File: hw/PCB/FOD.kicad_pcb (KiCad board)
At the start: 2 copper layers, 82.5 x 29 mm, 44 parts, among them J1 USB_B_Micro, J2 I2C, J3 I2C, J4 Programmer, J5 Micro_SD_Card_Det, J6 U.FL, Q1 PMV16XNR, Q2 PMV16XNR, SW1 Reset_push, U1 SAMD21G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

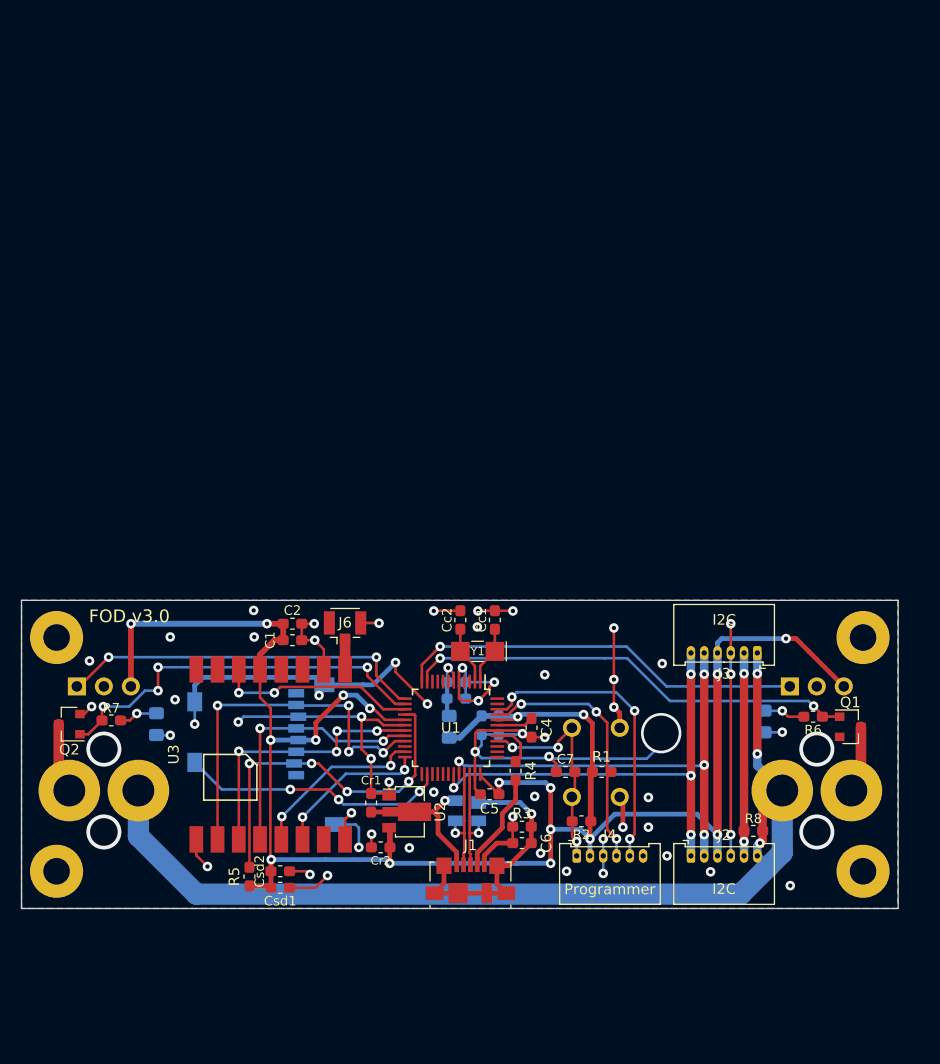
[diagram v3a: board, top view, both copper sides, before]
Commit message: FOD's new PCB version.
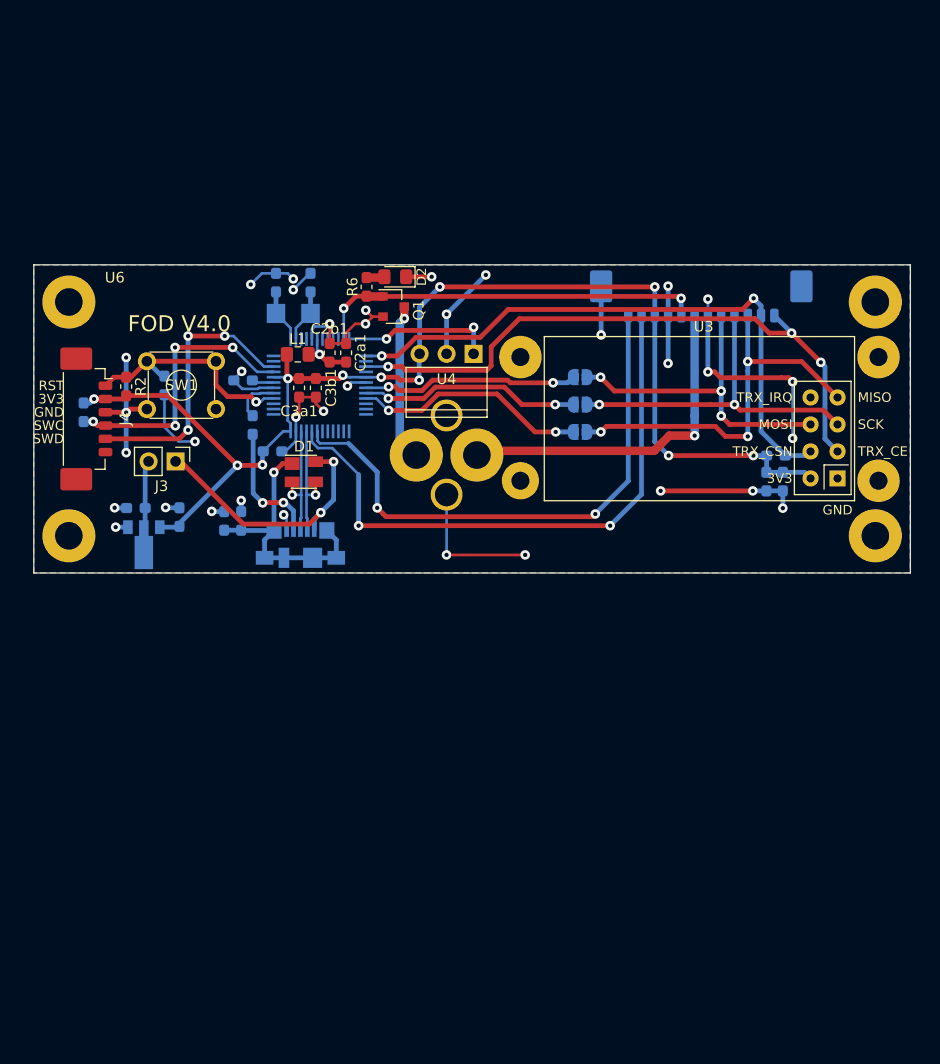
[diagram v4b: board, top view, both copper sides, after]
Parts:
- removed C1, Csd1: 10uF, Capacitor_SMD:C_0603_1608Metric_Pad1.05x0.95mm_HandSolder
- removed C2: 0.1uF, Capacitor_SMD:C_0603_1608Metric_Pad1.05x0.95mm_HandSolder
- removed Csd2: 100nF, Capacitor_SMD:C_0603_1608Metric_Pad1.05x0.95mm_HandSolder
- removed D3: LED, Diode_SMD:D_0805_2012Metric_Pad1.15x1.40mm_HandSolder
- removed J5: Micro_SD_Card_Det, SD:microSD_socket
- removed J6: U.FL, Connector_Coaxial:U.FL_Hirose_U.FL-R-SMT-1_Vertical
- removed Q2: PMV16XNR, Package_TO_SOT_SMD:SOT-23
- removed R5: 100k, Resistor_SMD:R_0603_1608Metric_Pad1.05x0.95mm_HandSolder
- removed R8: 0, Resistor_SMD:R_0603_1608Metric_Pad1.05x0.95mm_HandSolder
- removed U5: AV4524, Interrupt:AV4524
- added Ct1: 0.1uF, Capacitor_SMD:C_0603_1608Metric_Pad1.05x0.95mm_HandSolder, B.Cu at (170.1, 68.8)
- added Ct2: 10uF, Capacitor_SMD:C_0603_1608Metric_Pad1.05x0.95mm_HandSolder, B.Cu at (171.7, 68.8)
- added JP1: Jumper, Jumper:SolderJumper-2_P1.3mm_Open_RoundedPad1.0x1.5mm, B.Cu at (152.6, 59.0)
- added JP2: Jumper, Jumper:SolderJumper-2_P1.3mm_Open_RoundedPad1.0x1.5mm, B.Cu at (152.6, 61.6)
- added JP3: Jumper, Jumper:SolderJumper-2_P1.3mm_Open_RoundedPad1.0x1.5mm, B.Cu at (152.6, 64.2)
- added REF**: OSHW-Symbol_6.7x6mm_SilkScreen, Symbol:OSHW-Symbol_6.7x6mm_SilkScreen, B.Cu at (111.8, 52.8)
- C2a1, C2b1, C3a1, C3b1, D1, D2, L1, SW1, U4: moved to F.Cu
- C4, C5, C6, C7, Cc1, Cc2, Cr1, Cr2, J1, R1, R3, R4, U1, U2, Y1: moved to B.Cu
- J2: value I2C -> Comm_port; footprint Connector_Molex:Molex_PicoBlade_53048-0610_1x06_P1.25mm_Horizontal -> Connector_Molex:Molex_PicoBlade_53398-1271_1x12-1MP_P1.25mm_Vertical; moved to B.Cu
- J3: value I2C -> Jumper; footprint Connector_Molex:Molex_PicoBlade_53048-0610_1x06_P1.25mm_Horizontal -> Connector_PinHeader_2.54mm:PinHeader_1x02_P2.54mm_Vertical
- J4: footprint Connector_Molex:Molex_PicoBlade_53048-0610_1x06_P1.25mm_Horizontal -> Connector_Molex:Molex_PicoBlade_53398-0671_1x06-1MP_P1.25mm_Vertical
- R7: value 330 -> 0; moved to B.Cu
- U3: value RFM69HCW -> NRF24L01_Breakout; footprint Transceptor:RFM69HCW -> RF_Module:nRF24L01_Breakout
- U6: footprint Interstage:Type-A -> Interstage:Type-A_middle_port
- moved R7 67.3 mm to (171.0, 66.4)
- moved J4 61.4 mm to (106.7, 62.9), turned to -90 degrees
- moved R1 59.3 mm to (105.8, 62.3), turned to -90 degrees
- moved U3 59.3 mm to (176.8, 68.5), turned to 180 degrees
- moved R2 59.3 mm to (109.8, 59.9), turned to 90 degrees
- moved Q1 58.4 mm to (135.0, 52.4)
- moved R6 58.3 mm to (132.5, 50.5), turned to 90 degrees
- moved J3 57.6 mm to (114.5, 66.9), turned to -90 degrees
- moved D2 54.4 mm to (135.2, 49.5), turned to 180 degrees
- moved SW1 52.8 mm to (111.8, 57.5), turned to 0 degrees
- moved C7 52.4 mm to (113.5, 59.8), turned to -90 degrees
- moved J2 52.1 mm to (164.0, 52.0)
- moved U4 46.8 mm to (140.0, 56.8)
- moved C4 42.5 mm to (120.8, 59.3), turned to 180 degrees
- moved C6 41.3 mm to (119.1, 72.5), turned to 90 degrees
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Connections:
- net /DPL_STA1 renamed /DPL_STA
- net /Deploy/PORT1 renamed /Deploy/PORT
- C3a1 pad 1: +3V3 -> /3V3
- C3b1 pad 1: +3V3 -> /3V3
- C5 pad 1: +3V3 -> /3V3
- Cr1 pad 1: /VUSB -> Net-(Cr1-Pad1)
- Cr2 pad 1: +3V3 -> /3V3
- J2 pad 3: +3V3 -> /3V3
- J2 pad 5: /VAUX2 -> /DPL_EN
- J3 pad 1: /VAUX -> /VUSB
- J3 pad 2: /VAUX2 -> Net-(Cr1-Pad1)
- J4 pad 2: +3V3 -> /3V3
- L1 pad 2: +3V3 -> /3V3
- Q1 pad 1: /DPL_EN1 -> /DPL_EN
- R1 pad 1: +3V3 -> /3V3
- R2 pad 1: +3V3 -> /3V3
- R6 pad 1: /DPL_EN1 -> /DPL_EN
- R7 pad 1: /DPL_EN2 -> /3V3
- R7 pad 2: Net-(D3-Pad2) -> /TRX_CSN
- U1 pad 11: /DPL_EN1 -> /DPL_EN
- U1 pad 13: /DPL_STA2 -> /TRX_CSN
- U1 pad 14: /DPL_EN2 -> Net-(U1-Pad14)
- U1 pad 15: /TRX_INT -> /TRX_CE
- U1 pad 16: /DL_NSS -> Net-(U1-Pad16)
- U1 pad 17: +3V3 -> /3V3
- U1 pad 19: /MOSI -> /uC_MOSI
- U1 pad 20: /SCK -> /uC_SCK
- U1 pad 21: /MISO -> /uC_MISO
- U1 pad 23: /TRX_NSS -> Net-(U1-Pad23)
- U1 pad 24: /TRX_RST -> Net-(U1-Pad24)
- U1 pad 36: +3V3 -> /3V3
- U1 pad 44: +3V3 -> /3V3
- U2 pad 2: /VUSB -> Net-(Cr1-Pad1)
- U2 pad 3: +3V3 -> /3V3
- U3 pad 2: /MISO -> /3V3
- U3 pad 3: /MOSI -> /TRX_CE
- U3 pad 4: /SCK -> /TRX_CSN
- U3 pad 5: /TRX_NSS -> /SCK
- U3 pad 6: /TRX_RST -> /MOSI
- U3 pad 7: /Communication/DIO5 -> /MISO
- U3 pad 8: GND -> /TRX_IRQ
- U4 pad 3: +3V3 -> /3V3
- U6 pad 3: /Deploy/PORT2 -> GND
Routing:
- net +3V3: track 192.6 -> 0.00 mm, vias 18 -> 0
- net /3V3: track 0.00 -> 117.3 mm, vias 0 -> 11
- net /VAUX: track 99.3 -> 32.8 mm, vias 3 -> 1
- net GND: track 192.2 -> 132.4 mm, vias 63 -> 35
- net /TRX_CE: track 0.00 -> 59.3 mm, vias 0 -> 3
- net /TRX_CSN: track 0.00 -> 57.3 mm, vias 0 -> 2
- net /DPL_EN1: track 42.7 -> 0.00 mm, vias 2 -> 0
- net /DPL_EN: track 0.00 -> 37.1 mm, vias 0 -> 2
- net /DPL_EN2: track 37.1 -> 0.00 mm, vias 4 -> 0
- net /DPL_STA2: track 34.6 -> 0.00 mm, vias 2 -> 0
- net /DL_NSS: track 33.7 -> 0.00 mm, vias 4 -> 0
- net /DL_CD: track 25.3 -> 0.00 mm, vias 3 -> 0
- net /DPL_STA: track 38.5 -> 14.7 mm, vias 1 -> 2
- net /uC_MISO: track 0.00 -> 22.1 mm, vias 0 -> 2
- net /uC_SCK: track 0.00 -> 20.8 mm, vias 0 -> 2
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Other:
- net class Power2: trace_width 0.55 -> 0.8
- board text added: "DPL_EN"
- board text added: "FOD V4.0"
- board text added: "MISO"
- board text added: "MOSI"
- board text added: "SCK"
- board text added: "TRX_CE"
- board text added: "TRX_CS"
- board text added: "TRX_CSN"
- board text added: "TRX_IRQ"
- board text removed: "FOD v3.0"
- board text removed: "PORT1"
- board text removed: "PORT2"
- board text removed: "RESET"
- board text removed: "VAUX2"
